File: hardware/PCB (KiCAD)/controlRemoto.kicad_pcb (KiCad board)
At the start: 2 copper layers, 125 x 41 mm, 22 parts, among them J1 Modulo SD, J2 Display Oled, J3 Bornera, Q1 2N3904, SW1 ARRIBA, SW2 IZQUIERDA, SW3 ABAJO, SW4 DERECHA, SW5 ENTER, SW6 ATRAS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

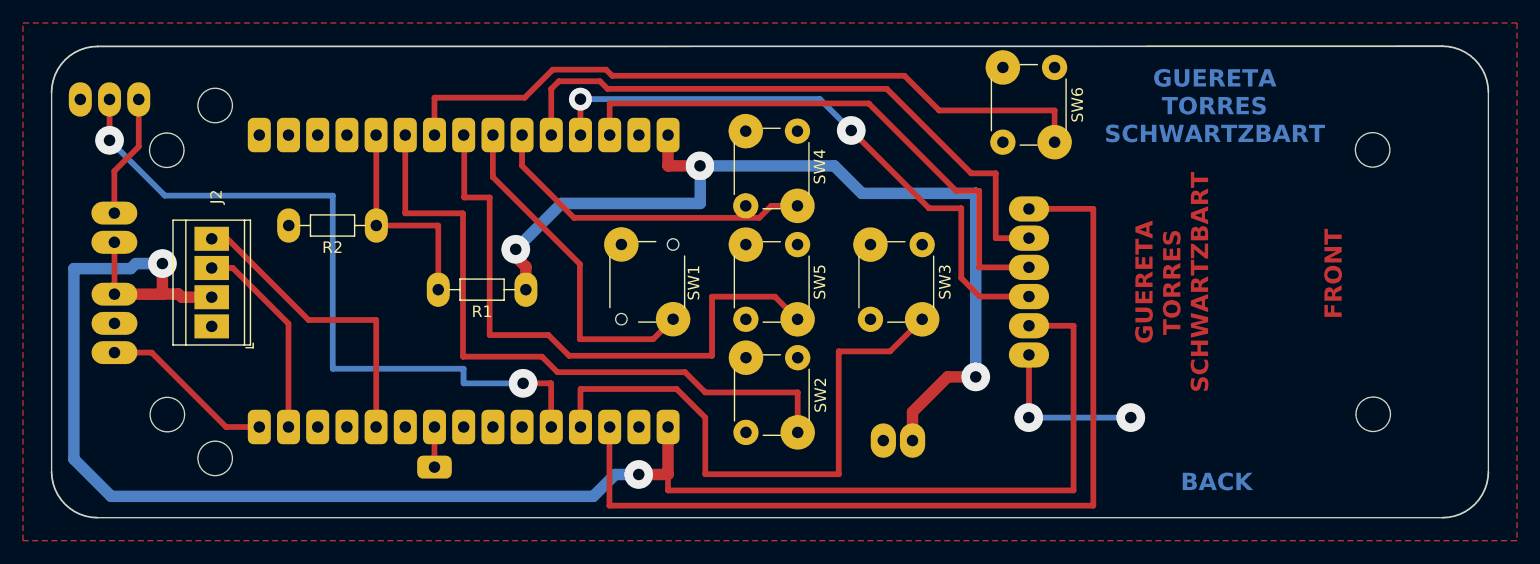
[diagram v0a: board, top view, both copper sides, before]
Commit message: Editando PCB
Haciendo pequeños cambios al PCB y subiendo los pdf invertidos para su fabricación.

Co-Authored-By: G4BY <105904708+G4BY0@users.noreply.github.com>
Co-Authored-By: joaquintorress <127200905+joaquintorress@users.noreply.github.com>
Co-Authored-By: schwartzbart <127200921+schwartzbart@users.noreply.github.com>
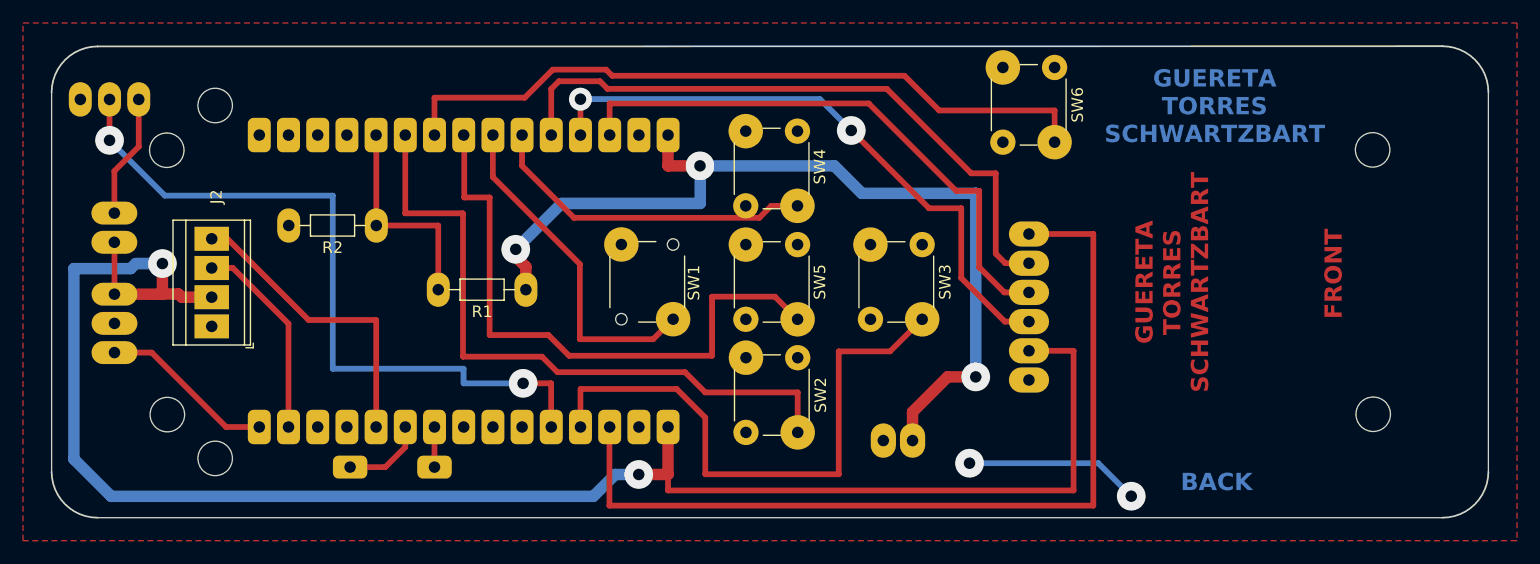
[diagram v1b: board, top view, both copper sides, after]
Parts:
- added ?: , , F.Cu at (107.1, 143.3)
- moved J1 2.18 mm to (166.2, 135.7)
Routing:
- net unconnected-(U3-D19-Pad10): track 0.00 -> 7.27 mm
- net D15: track 80.3 -> 78.2 mm
- net 3V3: track 153.0 -> 150.8 mm
- net D14: track 54.8 -> 56.5 mm
- net GND: track 14.3 -> 15.3 mm
- net D13: track 49.0 -> 49.9 mm
- net D12: track 52.8 -> 53.7 mm
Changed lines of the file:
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@@
       (sketchpadsonfab false)
       (subtractmaskfromsilk false)
-      (outputformat 1)
+      (outputformat 4)
       (mirror false)
-      (drillshape 0)
+      (drillshape 2)
       (scaleselection 1)
-      (outputdirectory "")
+      (outputdirectory "./")
     )
   )
@@
     (pad "15" thru_hole roundrect (at 0 0 180) (size 3 2) (drill 1) (layers "*.Cu" "B.Mask") (remove_unused_layers) (zone_layer_connections) (roundrect_rratio 0.25)
       (net 6 "unconnected-(U3-D18-Pad9)") (pinfunction "D23") (pintype "bidirectional"))
+  )
+  (footprint "" (layer "F.Cu")
+    (at 107.14 143.29)
+    (fp_text reference "" (at 0 0) (layer "F.SilkS")
+        (effects (font (size 1.27 1.27) (thickness 0.15)))
+    )
+    (fp_text value "" (at 0 0) (layer "F.SilkS")
+        (effects (font (size 1.27 1.27) (thickness 0.15)))
+    )
+    (pad "15" thru_hole roundrect (at 0 0 180) (size 3 2) (drill 1) (layers "*.Cu" "B.Mask") (remove_unused_layers) (zone_layer_connections) (roundrect_rratio 0.25)
+      (net 7 "unconnected-(U3-D19-Pad10)") (pinfunction "D23") (pintype "bidirectional"))
   )
   (footprint "" (layer "F.Cu")
@@
   )
   (footprint "TerminalBlock_TE-Connectivity:TerminalBlock_TE_282834-6_1x06_P2.54mm_Horizontal" (layer "B.Cu")
-    (at 166.2 133.53 90)
+    (at 166.2 135.71 90)
     (descr "Terminal Block TE 282834-6, 6 pins, pitch 2.54mm, size 15.7x6.5mm^2, drill diamater 1.1mm, pad diameter 2.1mm, see http://www.te.com/commerce/DocumentDelivery/DDEController?Action=showdoc&DocId=Customer+Drawing%7F282834%7FC1%7Fpdf%7FEnglish%7FENG_CD_282834_C1.pdf, script-generated using https://github.com/pointhi/kicad-footprint-generator/scripts/TerminalBlock_TE-Connectivity")
     (tags "THT Terminal Block TE 282834-6 pitch 2.54mm size 15.7x6.5mm^2 drill 1.1mm pad 2.1mm")
@@
   (gr_line (start 196.15 115.69) (end 196.15 106.69)
     (stroke (width 0.15) (type default)) (layer "Dwgs.User"))
+  (gr_line (start 166.22 141.345) (end 166.22 117.355)
+    (stroke (width 0.2) (type default)) (layer "Dwgs.User"))
   (gr_arc (start 82.67 149.69) (mid 79.841573 148.518427) (end 78.67 145.69)
     (stroke (width 0.15) (type default)) (layer "Dwgs.User"))
@@
   (segment (start 88.75 115.41) (end 86.63 117.53) (width 0.5) (layer "F.Cu") (net 1))
   (segment (start 88.75 111.3) (end 88.75 115.41) (width 0.5) (layer "F.Cu") (net 1))
-  (segment (start 166.2 138.96) (end 166.2 133.53) (width 0.5) (layer "F.Cu") (net 2))
-  (segment (start 166.18 138.98) (end 166.2 138.96) (width 0.5) (layer "F.Cu") (net 2))
-  (via (at 175.06 138.98) (size 2.5) (drill 1) (layers "F.Cu" "B.Cu") (net 2))
-  (via (at 166.18 138.98) (size 2.5) (drill 1) (layers "F.Cu" "B.Cu") (net 2))
-  (segment (start 175.06 138.98) (end 166.18 138.98) (width 0.5) (layer "B.Cu") (net 2))
+  (via (at 175.1 145.82) (size 2.5) (drill 1) (layers "F.Cu" "B.Cu") (net 2))
+  (via (at 161.03 142.95) (size 2.5) (drill 1) (layers "F.Cu" "B.Cu") (net 2))
+  (segment (start 172.23 142.95) (end 175.1 145.82) (width 0.5) (layer "B.Cu") (net 2))
+  (segment (start 161.03 142.95) (end 172.23 142.95) (width 0.5) (layer "B.Cu") (net 2))
   (segment (start 134.8 117.07) (end 134.8 114.4) (width 1) (layer "F.Cu") (net 3))
   (segment (start 134.81 117.08) (end 134.8 117.07) (width 1) (layer "F.Cu") (net 3))
@@
   (segment (start 137.6 117.1) (end 137.58 117.08) (width 1) (layer "B.Cu") (net 3))
   (segment (start 114.48 143.29) (end 114.48 139.8) (width 0.5) (layer "F.Cu") (net 6))
+  (segment (start 111.94 139.8) (end 111.94 141.55) (width 0.5) (layer "F.Cu") (net 7))
+  (segment (start 111.94 141.55) (end 110.2 143.29) (width 0.5) (layer "F.Cu") (net 7))
+  (segment (start 110.2 143.29) (end 107.14 143.29) (width 0.5) (layer "F.Cu") (net 7))
   (segment (start 90.8 128.245) (end 86.64 128.245) (width 1) (layer "F.Cu") (net 10))
   (segment (start 92.485 128.505) (end 95.1 128.505) (width 1) (layer "F.Cu") (net 10))
   (segment (start 90.81 125.58) (end 90.81 128.235) (width 1) (layer "F.Cu") (net 10))
+  (segment (start 170.08 133.19) (end 170.08 145.32) (width 0.5) (layer "F.Cu") (net 10))
+  (segment (start 166.2 133.17) (end 170.06 133.17) (width 0.5) (layer "F.Cu") (net 10))
   (segment (start 86.64 128.245) (end 86.64 123.74) (width 0.5) (layer "F.Cu") (net 10))
   (segment (start 90.81 128.235) (end 90.815 128.23) (width 1) (layer "F.Cu") (net 10))
   (segment (start 86.64 123.74) (end 86.63 123.73) (width 0.5) (layer "F.Cu") (net 10))
   (segment (start 132.25 143.93) (end 134.8 143.93) (width 1) (layer "F.Cu") (net 10))
-  (segment (start 166.2 130.99) (end 170.08 130.99) (width 0.5) (layer "F.Cu") (net 10))
   (segment (start 90.815 128.23) (end 92.21 128.23) (width 1) (layer "F.Cu") (net 10))
+  (segment (start 170.08 145.32) (end 134.8 145.32) (width 0.5) (layer "F.Cu") (net 10))
   (segment (start 92.21 128.23) (end 92.485 128.505) (width 1) (layer "F.Cu") (net 10))
+  (segment (start 170.06 133.17) (end 170.08 133.19) (width 0.5) (layer "F.Cu") (net 10))
+  (segment (start 134.8 139.8) (end 134.8 143.93) (width 1) (layer "F.Cu") (net 10))
   (segment (start 134.8 145.32) (end 134.8 143.93) (width 0.5) (layer "F.Cu") (net 10))
-  (segment (start 134.8 139.8) (end 134.8 143.93) (width 1) (layer "F.Cu") (net 10))
-  (segment (start 170.08 130.99) (end 170.08 145.32) (width 0.5) (layer "F.Cu") (net 10))
-  (segment (start 170.08 145.32) (end 134.8 145.32) (width 0.5) (layer "F.Cu") (net 10))
   (via (at 132.25 143.93) (size 2.5) (drill 1) (layers "F.Cu" "B.Cu") (free) (net 10))
   (via (at 90.81 125.58) (size 2.5) (drill 1) (layers "F.Cu" "B.Cu") (free) (net 10))
@@
   (segment (start 86.35 145.83) (end 83.11 142.59) (width 1) (layer "B.Cu") (net 10))
   (segment (start 83.11 142.59) (end 83.11 126.02) (width 1) (layer "B.Cu") (net 10))
+  (segment (start 164.1 130.63) (end 160.31 126.84) (width 0.5) (layer "F.Cu") (net 16))
   (segment (start 160.31 120.77) (end 157.51 120.77) (width 0.5) (layer "F.Cu") (net 16))
-  (segment (start 166.2 128.45) (end 161.92 128.45) (width 0.5) (layer "F.Cu") (net 16))
-  (segment (start 161.92 128.45) (end 160.31 126.84) (width 0.5) (layer "F.Cu") (net 16))
+  (segment (start 166.2 130.63) (end 164.1 130.63) (width 0.5) (layer "F.Cu") (net 16))
   (segment (start 160.31 126.84) (end 160.31 120.77) (width 0.5) (layer "F.Cu") (net 16))
   (segment (start 127.18 111.2795) (end 127.18 114.4) (width 0.5) (layer "F.Cu") (net 16))
@@
   (segment (start 148.01 111.27) (end 150.74 114) (width 0.5) (layer "B.Cu") (net 16))
   (segment (start 161.88 125.91) (end 161.87 125.92) (width 0.5) (layer "F.Cu") (net 17))
+  (segment (start 166.2 128.09) (end 164.06 128.09) (width 0.5) (layer "F.Cu") (net 17))
   (segment (start 161.87 119.26) (end 159.87 119.26) (width 0.5) (layer "F.Cu") (net 17))
-  (segment (start 166.2 125.91) (end 161.88 125.91) (width 0.5) (layer "F.Cu") (net 17))
   (segment (start 161.87 125.92) (end 161.87 119.26) (width 0.5) (layer "F.Cu") (net 17))
   (segment (start 129.72 111.65) (end 129.72 114.4) (width 0.5) (layer "F.Cu") (net 17))
   (segment (start 159.87 119.26) (end 152.26 111.65) (width 0.5) (layer "F.Cu") (net 17))
   (segment (start 152.26 111.65) (end 129.72 111.65) (width 0.5) (layer "F.Cu") (net 17))
+  (segment (start 164.06 128.09) (end 161.88 125.91) (width 0.5) (layer "F.Cu") (net 17))
   (segment (start 163.31 117.73) (end 161.18 117.73) (width 0.5) (layer "F.Cu") (net 18))
-  (segment (start 166.2 123.37) (end 163.31 123.37) (width 0.5) (layer "F.Cu") (net 18))
+  (segment (start 124.64 110.38) (end 124.64 114.4) (width 0.5) (layer "F.Cu") (net 18))
+  (segment (start 128.88 109.72) (end 125.3 109.72) (width 0.5) (layer "F.Cu") (net 18))
   (segment (start 153.83 110.38) (end 129.54 110.38) (width 0.5) (layer "F.Cu") (net 18))
+  (segment (start 166.2 125.55) (end 164.14 125.55) (width 0.5) (layer "F.Cu") (net 18))
+  (segment (start 161.18 117.73) (end 153.83 110.38) (width 0.5) (layer "F.Cu") (net 18))
+  (segment (start 163.31 124.72) (end 163.31 117.73) (width 0.5) (layer "F.Cu") (net 18))
   (segment (start 125.3 109.72) (end 124.64 110.38) (width 0.5) (layer "F.Cu") (net 18))
-  (segment (start 163.31 123.37) (end 163.31 117.73) (width 0.5) (layer "F.Cu") (net 18))
-  (segment (start 128.88 109.72) (end 125.3 109.72) (width 0.5) (layer "F.Cu") (net 18))
+  (segment (start 164.14 125.55) (end 163.31 124.72) (width 0.5) (layer "F.Cu") (net 18))
   (segment (start 129.54 110.38) (end 128.88 109.72) (width 0.5) (layer "F.Cu") (net 18))
-  (segment (start 161.18 117.73) (end 153.83 110.38) (width 0.5) (layer "F.Cu") (net 18))
-  (segment (start 124.64 110.38) (end 124.64 114.4) (width 0.5) (layer "F.Cu") (net 18))
-  (segment (start 171.8 120.82) (end 171.8 146.64) (width 0.5) (layer "F.Cu") (net 19))
   (segment (start 171.8 146.64) (end 129.7 146.64) (width 0.5) (layer "F.Cu") (net 19))
+  (segment (start 166.2 123.01) (end 171.8 123.01) (width 0.5) (layer "F.Cu") (net 19))
   (segment (start 129.7 146.64) (end 129.7 139.82) (width 0.5) (layer "F.Cu") (net 19))
-  (segment (start 166.2 120.83) (end 166.85 120.83) (width 0.5) (layer "F.Cu") (net 19))
-  (segment (start 166.85 120.83) (end 166.86 120.82) (width 0.5) (layer "F.Cu") (net 19))
-  (segment (start 166.86 120.82) (end 171.8 120.82) (width 0.5) (layer "F.Cu") (net 19))
+  (segment (start 171.8 123.01) (end 171.8 146.64) (width 0.5) (layer "F.Cu") (net 19))
   (segment (start 96.015 125.96) (end 96.93 125.96) (width 0.5) (layer "F.Cu") (net 20))
   (segment (start 101.78 130.81) (end 101.78 139.8) (width 0.5) (layer "F.Cu") (net 20))

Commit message: Añadiendo archivos STL's y PCB
Los respectivos STL del gabinete y keycaps y también el KiCAD del PCB.

Co-Authored-By: G4BY <105904708+G4BY0@users.noreply.github.com>
Co-Authored-By: joaquintorress <127200905+joaquintorress@users.noreply.github.com>
Co-Authored-By: schwartzbart <127200921+schwartzbart@users.noreply.github.com>
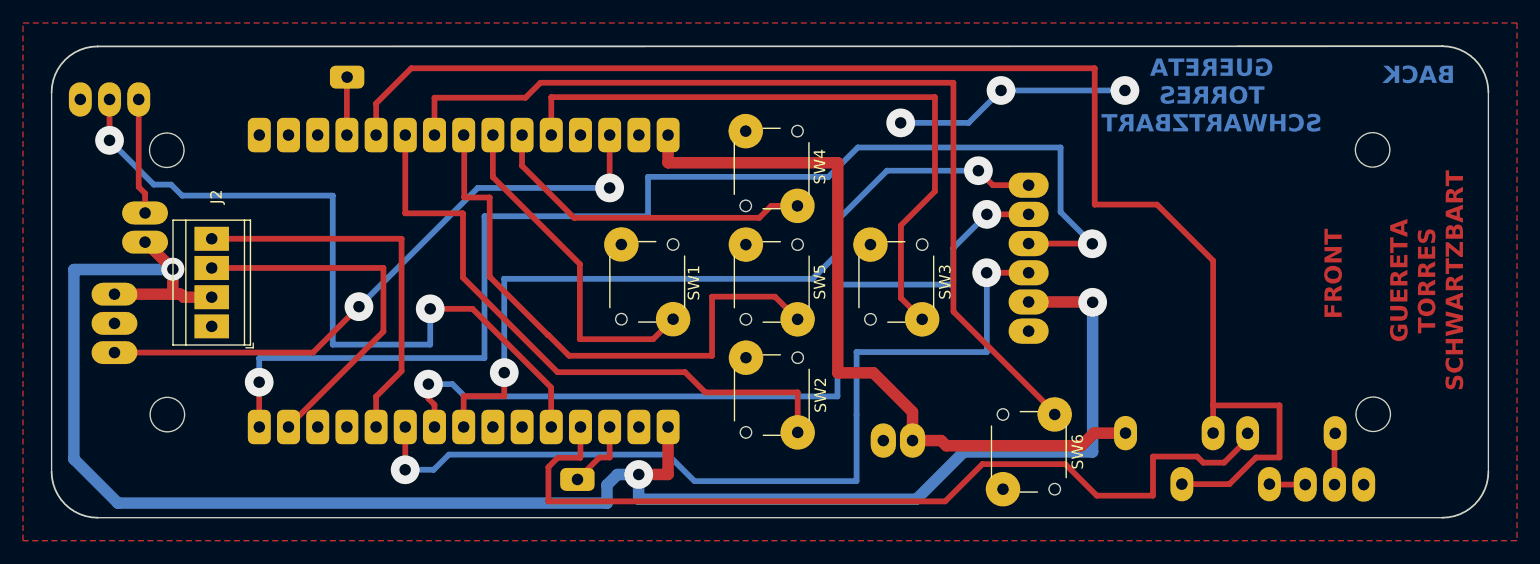
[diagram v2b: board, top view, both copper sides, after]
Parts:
- removed the ? at (114.5, 143.3)
- removed the ? at (107.1, 143.3)
- removed the ? at (95.4, 111.8)
- removed the ? at (95.4, 142.5)
- added ?: , , F.Cu at (126.9, 144.4)
- added ?: , , F.Cu at (106.9, 109.4)
- added Q2: BC546, Package_TO_SOT_THT:TO-92_Inline_Wide, B.Cu at (190.2, 144.8)
- added R3: 630000, Resistor_THT:R_Axial_DIN0204_L3.6mm_D1.6mm_P7.62mm_Horizontal, B.Cu at (185.2, 140.3)
- R1, R2: value 1000 -> 10000; moved to B.Cu
- moved R2 73.6 mm to (179.5, 144.8), turned to 0 degrees
- moved R1 53.6 mm to (174.6, 140.3), turned to 0 degrees
- moved SW6 30.2 mm to (168.4, 138.7)
- moved J1 4.25 mm to (166.2, 131.5)
- moved D1 2.67 mm to (89.3, 121.2)
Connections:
- J1 pad 3: D12 -> D19
- J1 pad 4: D13 -> D23
- J1 pad 5: D14 -> D18
- J1 pad 6: D15 -> D5
- R2 pad 2: GND -> Net-(Q2-C)
- SW3 pad 1: D2 -> D14
- U2 pad 1: D23 -> D13
- U3 pad 10: unconnected-(U3-D19-Pad10) -> D19
- U3 pad 19: unconnected-(U3-D34-Pad19) -> Charger1
- U3 pad 2: (no net) -> GND
- U3 pad 27: D12 -> unconnected-(U3-D12-Pad27)
- U3 pad 3: D15 -> Charger2
- U3 pad 8: unconnected-(U3-D5-Pad8) -> D5
- U3 pad 9: unconnected-(U3-D18-Pad9) -> D18
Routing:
- net D35: track 18.8 -> 125.5 mm
- net D23: track 15.3 -> 107.6 mm, vias 0 -> 2
- net D15: track 78.2 -> 0.00 mm
- net D19: track 0.00 -> 77.6 mm, vias 0 -> 2
- net D18: track 0.00 -> 70.6 mm, vias 0 -> 2
- net D5: track 0.00 -> 68.2 mm, vias 0 -> 2
- net D12: track 53.7 -> 0.00 mm, vias 2 -> 0
- net D2: track 50.8 -> 77.0 mm
- net D33: track 62.4 -> 81.3 mm
- net +3V8: track 79.9 -> 65.0 mm, vias 3 -> 0
- net D22: track 17.7 -> 32.2 mm
- net 3V3: track 150.8 -> 160.6 mm, vias 2 -> 3
- net D21: track 26.5 -> 33.8 mm
- net unconnected-(U3-D19-Pad10): track 7.27 -> 0.00 mm
- net Charger2: track 0.00 -> 6.24 mm
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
